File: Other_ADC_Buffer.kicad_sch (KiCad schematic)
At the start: 15 parts, among them U10 TLV6001DCK, U11 TLV6001DCK, U12 TLV6001DCK

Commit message: Adjusted cap sizes, 0603 for all need hand soldering, 0402 where possible, 0804 as needed
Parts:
- C32, C33, C34: footprint Capacitor_SMD:C_0402_1005Metric_Pad0.74x0.62mm_HandSolder -> Capacitor_SMD:C_0603_1608Metric
- R32, R33, R34, R35, R36, R37: footprint Resistor_SMD:R_0402_1005Metric_Pad0.72x0.64mm_HandSolder -> Resistor_SMD:R_0603_1608Metric
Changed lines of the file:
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@@
 			)
 		)
-		(property "Footprint" "Capacitor_SMD:C_0402_1005Metric_Pad0.74x0.62mm_HandSolder"
+		(property "Footprint" "Capacitor_SMD:C_0603_1608Metric"
 			(at 94.9452 157.48 0)
 			(effects
@@
 			)
 		)
-		(property "Footprint" "Resistor_SMD:R_0402_1005Metric_Pad0.72x0.64mm_HandSolder"
+		(property "Footprint" "Resistor_SMD:R_0603_1608Metric"
 			(at 82.55 47.498 90)
 			(effects
@@
 			)
 		)
-		(property "Footprint" "Capacitor_SMD:C_0402_1005Metric_Pad0.74x0.62mm_HandSolder"
+		(property "Footprint" "Capacitor_SMD:C_0603_1608Metric"
 			(at 94.9452 55.88 0)
 			(effects
@@
 			)
 		)
-		(property "Footprint" "Resistor_SMD:R_0402_1005Metric_Pad0.72x0.64mm_HandSolder"
+		(property "Footprint" "Resistor_SMD:R_0603_1608Metric"
 			(at 86.36 98.298 90)
 			(effects
@@
 			)
 		)
-		(property "Footprint" "Resistor_SMD:R_0402_1005Metric_Pad0.72x0.64mm_HandSolder"
+		(property "Footprint" "Resistor_SMD:R_0603_1608Metric"
 			(at 80.518 91.44 90)
 			(effects
@@
 			)
 		)
-		(property "Footprint" "Capacitor_SMD:C_0402_1005Metric_Pad0.74x0.62mm_HandSolder"
+		(property "Footprint" "Capacitor_SMD:C_0603_1608Metric"
 			(at 94.9452 106.68 0)
 			(effects
@@
 			)
 		)
-		(property "Footprint" "Resistor_SMD:R_0402_1005Metric_Pad0.72x0.64mm_HandSolder"
+		(property "Footprint" "Resistor_SMD:R_0603_1608Metric"
 			(at 86.36 149.098 90)
 			(effects
@@
 			)
 		)
-		(property "Footprint" "Resistor_SMD:R_0402_1005Metric_Pad0.72x0.64mm_HandSolder"
+		(property "Footprint" "Resistor_SMD:R_0603_1608Metric"
 			(at 90.678 52.07 90)
 			(effects
@@
 			)
 		)
-		(property "Footprint" "Resistor_SMD:R_0402_1005Metric_Pad0.72x0.64mm_HandSolder"
+		(property "Footprint" "Resistor_SMD:R_0603_1608Metric"
 			(at 80.518 142.24 90)
 			(effects

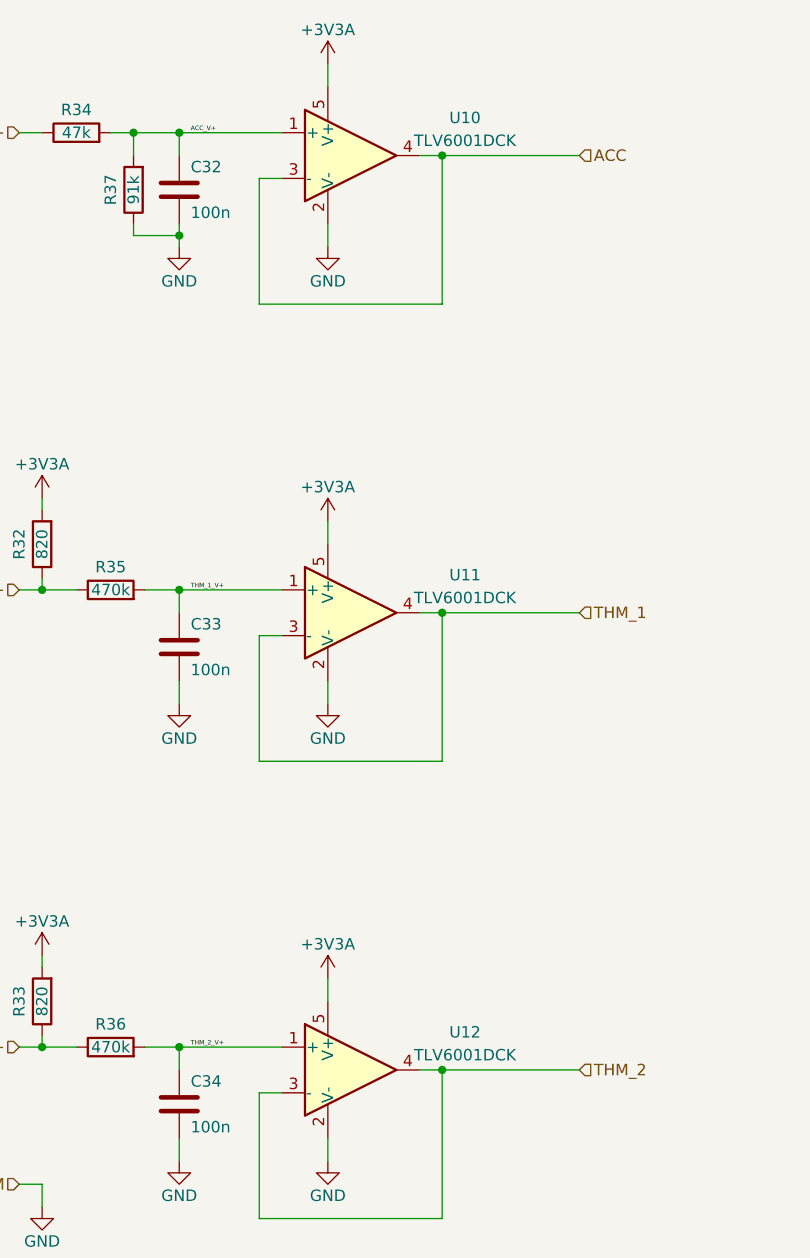
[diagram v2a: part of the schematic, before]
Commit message: Changed op Amp, need to reroute, need to re-asses capacitor situation since || 0.1 and 1 is dumb. Just use 2 1s in that case.
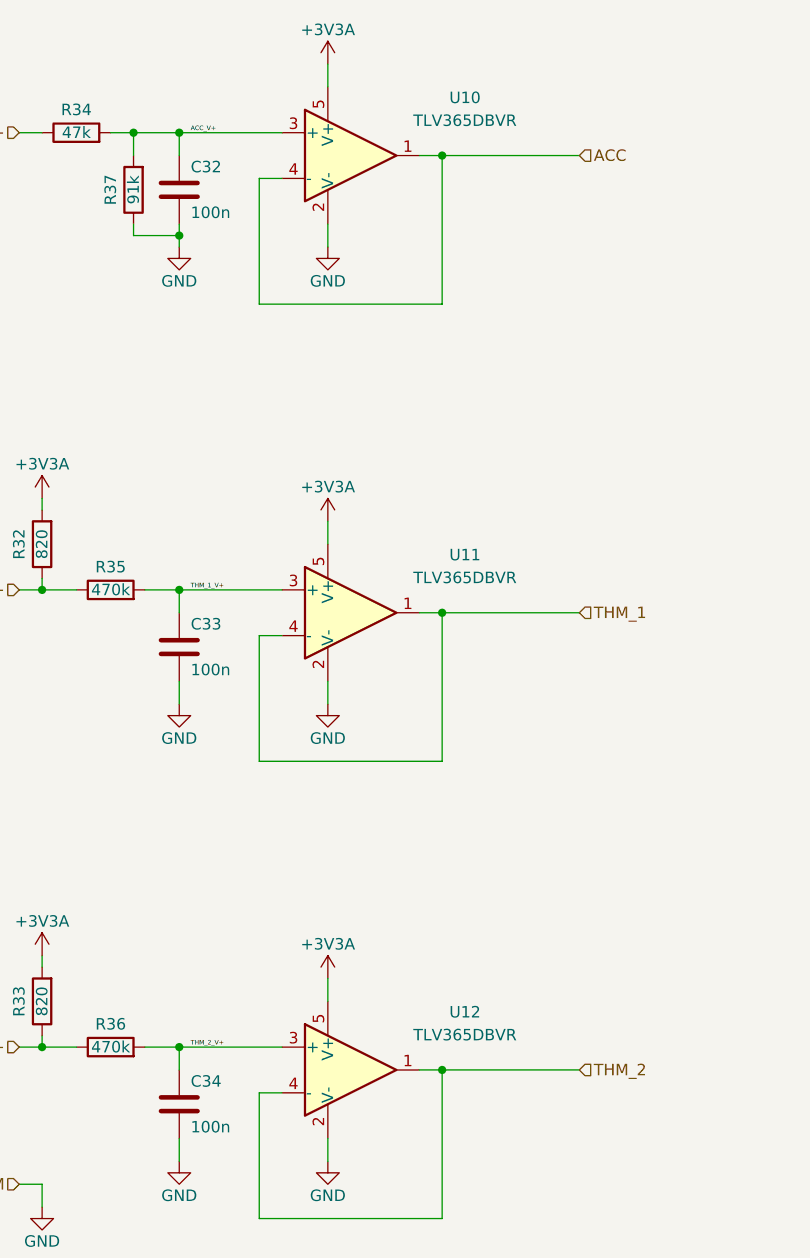
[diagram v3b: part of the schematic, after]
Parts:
- removed U10, U11, U12: TLV6001DCK, Package_TO_SOT_SMD:SOT-353_SC-70-5, symbol Amplifier_Operational:TLV6001DCK
- added U10, U11, U12: TLV365DBVR, Package_TO_SOT_SMD:SOT-23-5, symbol User_OpAmp:TLV365DBVR
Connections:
- net +3V3A: now also U10.5 (V+), U11.5 (V+), U12.5 (V+)
- net ACC: now also U10.1, U10.4 (-)
- net ACC_V+: now also U10.3 (+)
- net GND: now also U10.2 (V-), U11.2 (V-), U12.2 (V-)
- net THM_1: now also U11.1, U11.4 (-)
- net THM_1_V+: now also U11.3 (+)
- net THM_2: now also U12.1, U12.4 (-)
- net THM_2_V+: now also U12.3 (+)

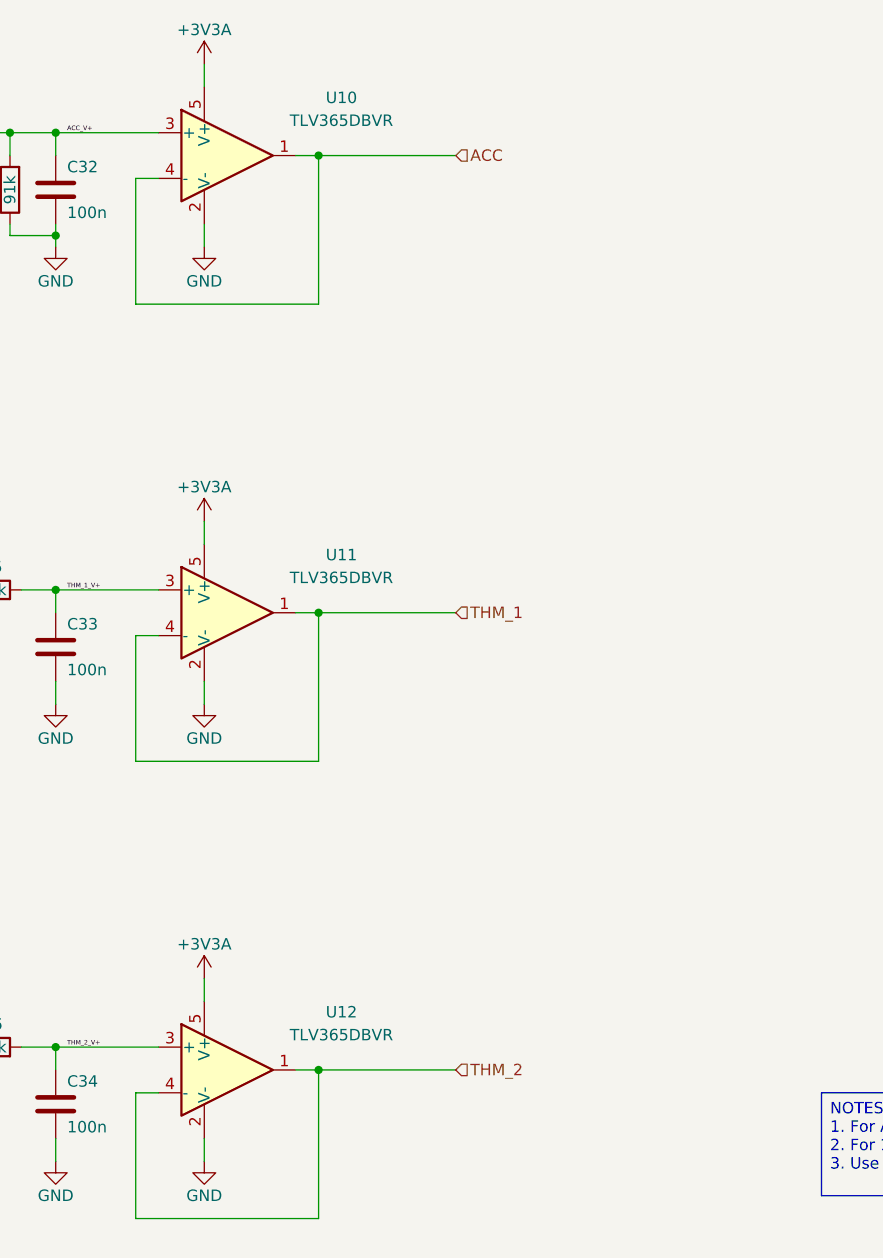
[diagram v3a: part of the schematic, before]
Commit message: Cheaper, smaller 10MHz Op Amp
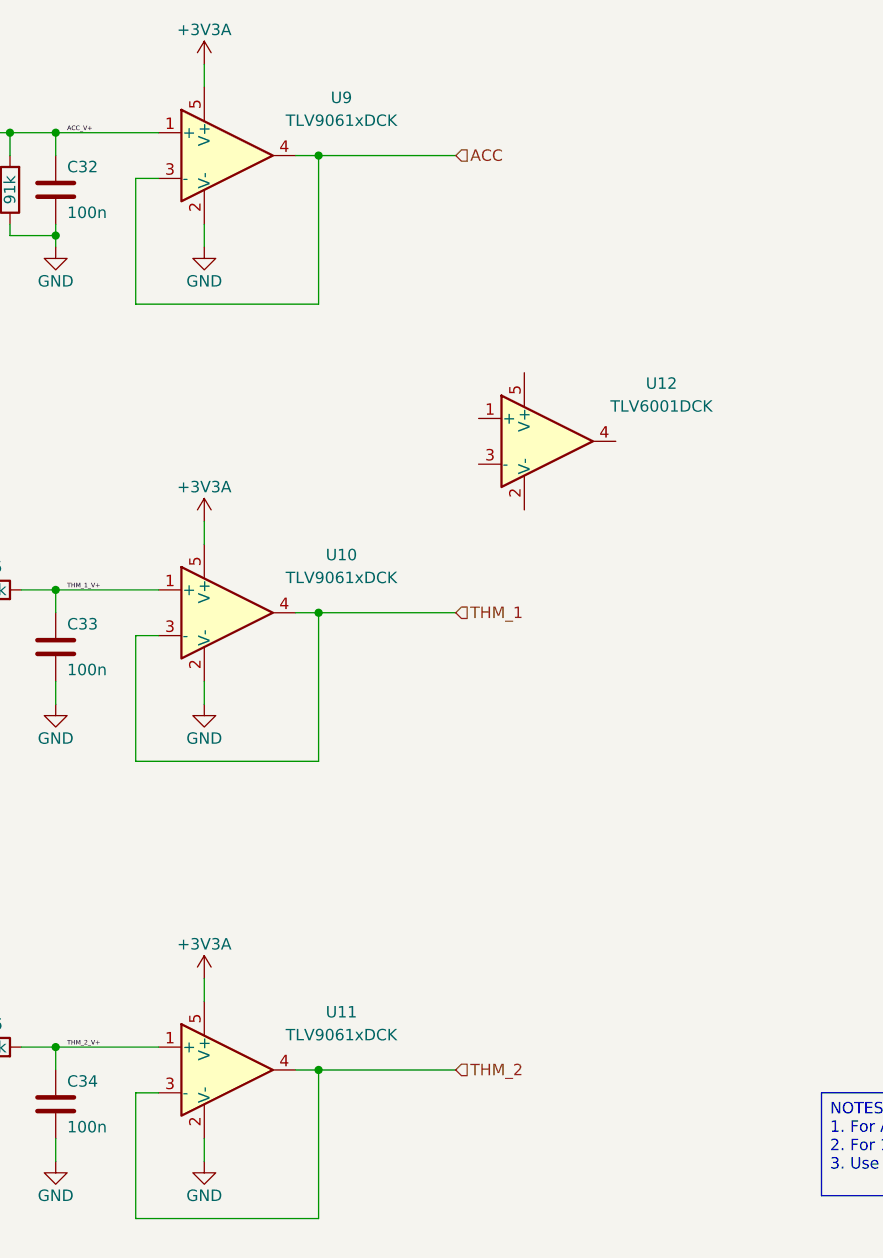
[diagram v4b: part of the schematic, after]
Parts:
- removed U10, U11, U12: TLV365DBVR, Package_TO_SOT_SMD:SOT-23-5, symbol User_OpAmp:TLV365DBVR
- added U10, U11, U9: TLV9061xDCK, Package_TO_SOT_SMD:SOT-353_SC-70-5, symbol Amplifier_Operational:TLV9061xDCK
- added U12: TLV6001DCK, Package_TO_SOT_SMD:SOT-353_SC-70-5, symbol Amplifier_Operational:TLV6001DCK
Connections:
- net +3V3A: now also U10.5 (V+), U11.5 (V+), U9.5 (V+)
- net ACC: now also U9.3 (-), U9.4
- net ACC_V+: now also U9.1 (+)
- net GND: now also U10.2 (V-), U11.2 (V-), U9.2 (V-)
- net THM_1: now also U10.3 (-), U10.4
- net THM_1_V+: now also U10.1 (+)
- net THM_2: now also U11.3 (-), U11.4
- net THM_2_V+: now also U11.1 (+)

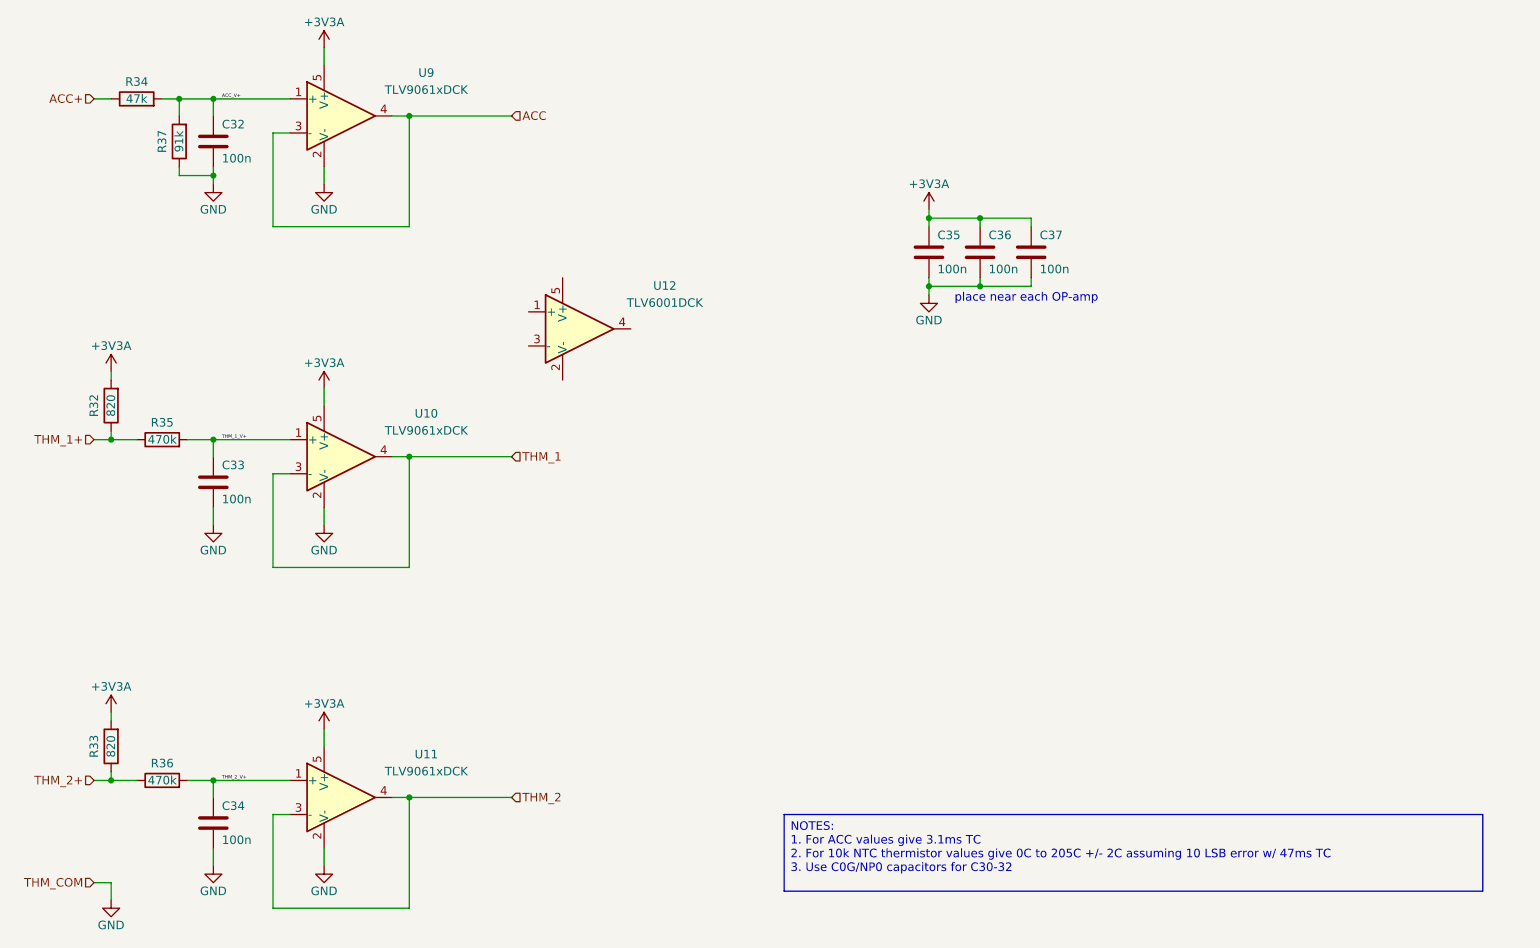
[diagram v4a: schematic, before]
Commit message: Updating all decoupling to 1u
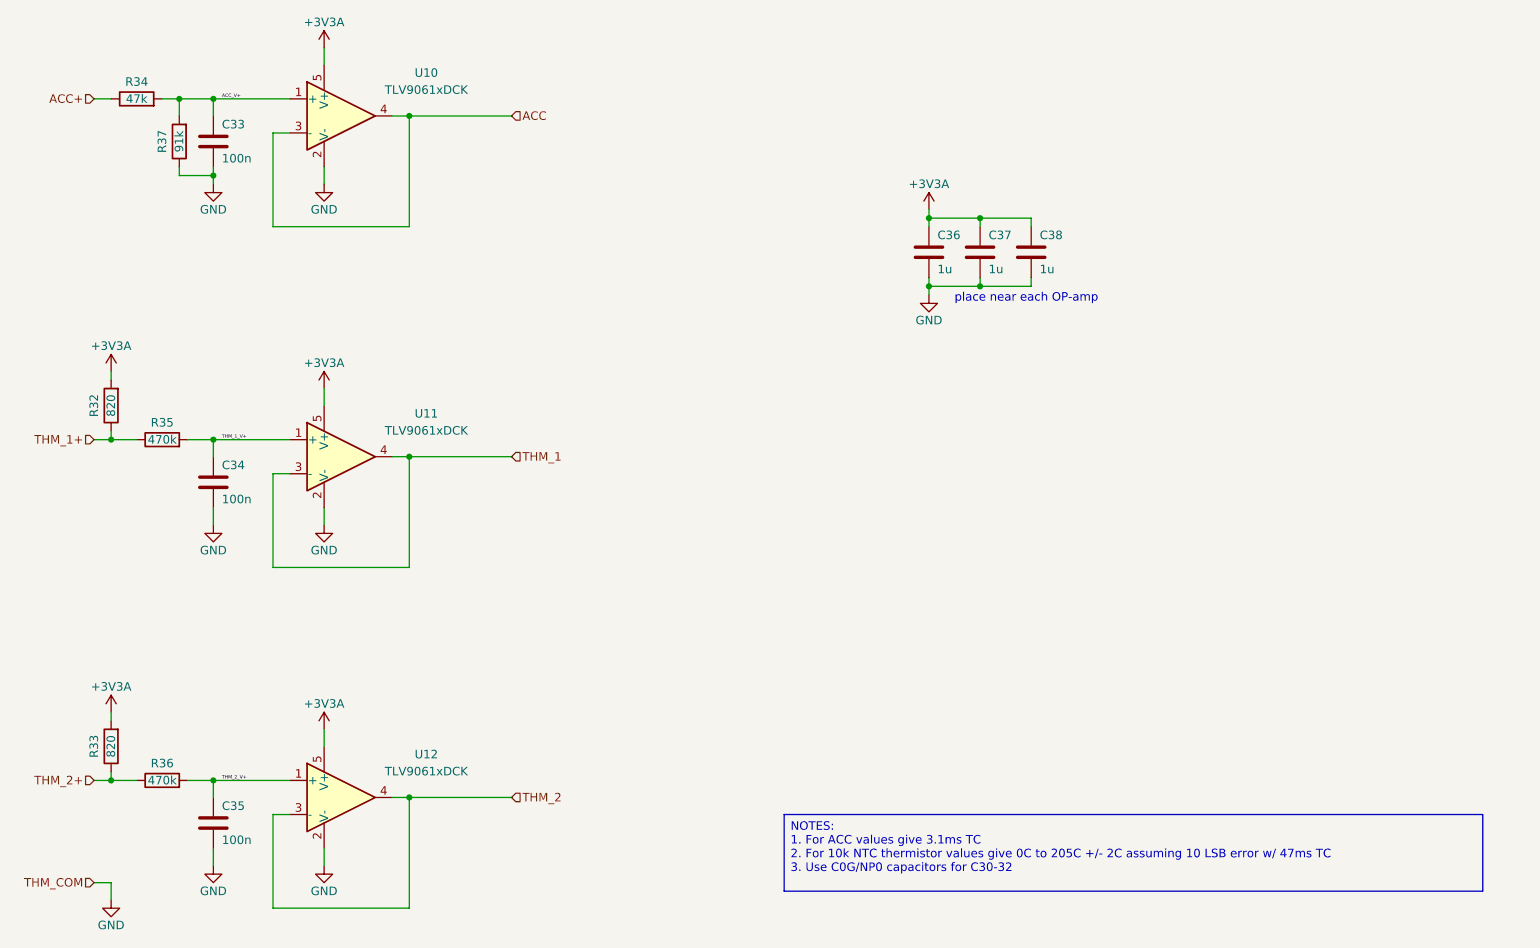
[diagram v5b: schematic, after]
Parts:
- removed C36: 100n, Capacitor_SMD:C_0402_1005Metric, symbol Device:C
- removed U12: TLV6001DCK, Package_TO_SOT_SMD:SOT-353_SC-70-5, symbol Amplifier_Operational:TLV6001DCK
- added C38: 1u, Capacitor_SMD:C_0402_1005Metric, symbol Device:C
- C36: renamed from C35; value 100n -> 1u
- C37: value 100n -> 1u
- renumbered C32 to C33, C33 to C34, C34 to C35, U9 to U10, U10 to U11, U11 to U12
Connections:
- net +3V3A: now also C38.1
- net GND: now also C38.2
